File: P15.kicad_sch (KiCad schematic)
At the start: 12 parts

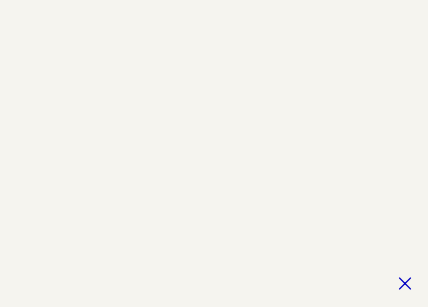
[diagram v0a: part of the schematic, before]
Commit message: fixing KiCad6 warnings
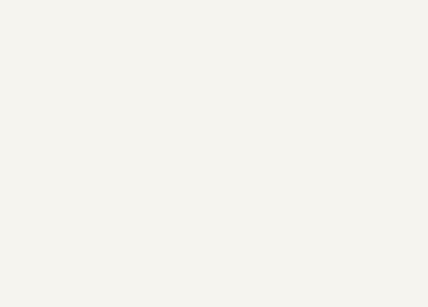
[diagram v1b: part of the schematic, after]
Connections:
- no-connect marks 20 -> 19
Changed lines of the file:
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@@
   (no_connect (at 36.83 78.74))
   (no_connect (at 49.53 36.83))
-  (no_connect (at 613.41 278.13))
   (no_connect (at 128.27 78.74))
   (no_connect (at 172.72 80.01))
